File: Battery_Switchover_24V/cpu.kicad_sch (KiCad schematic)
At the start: 35 parts, among them J1 USB_C_Receptacle_USB2.0_14P, M1 Fan, Q1 NPN, SW1 SW_Push, U1 OPA2197xD, U2 OPA2197xD, U3 LPC11U14FBD48-201, Y1 12.000MHz

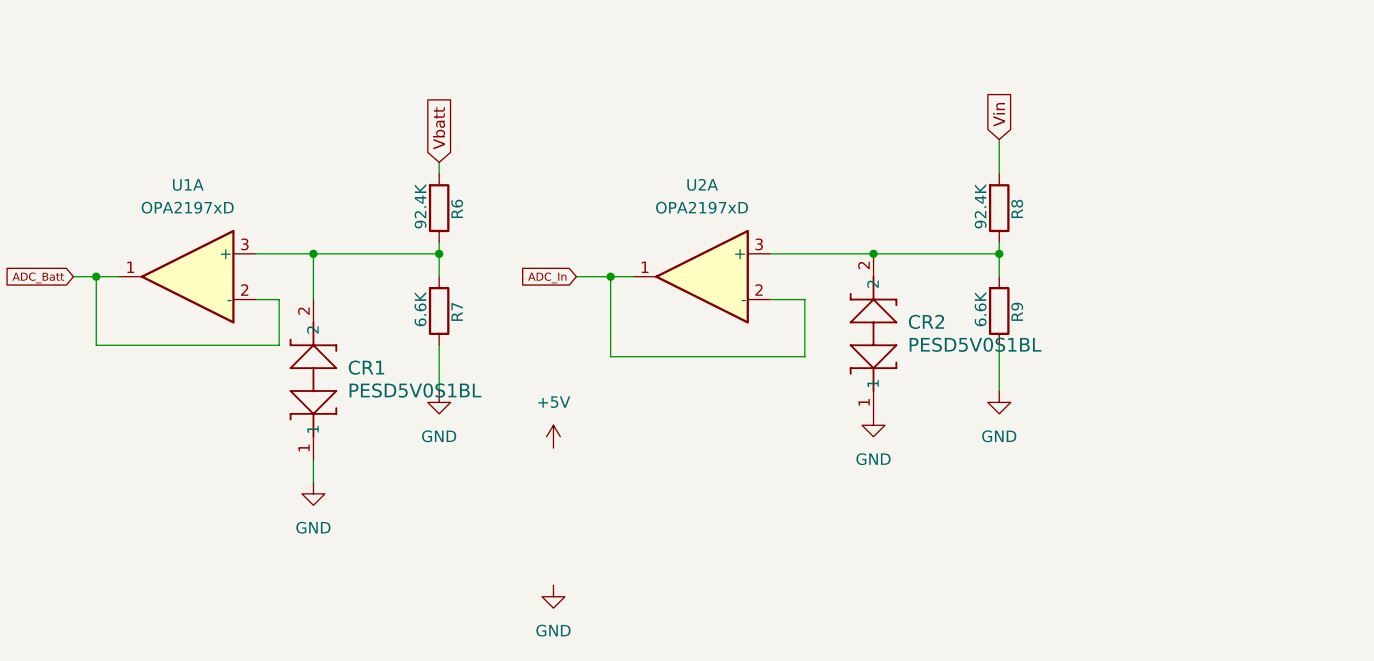
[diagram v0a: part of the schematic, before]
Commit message: Added common mode chokes for input and output of the load fixed the corrupted board
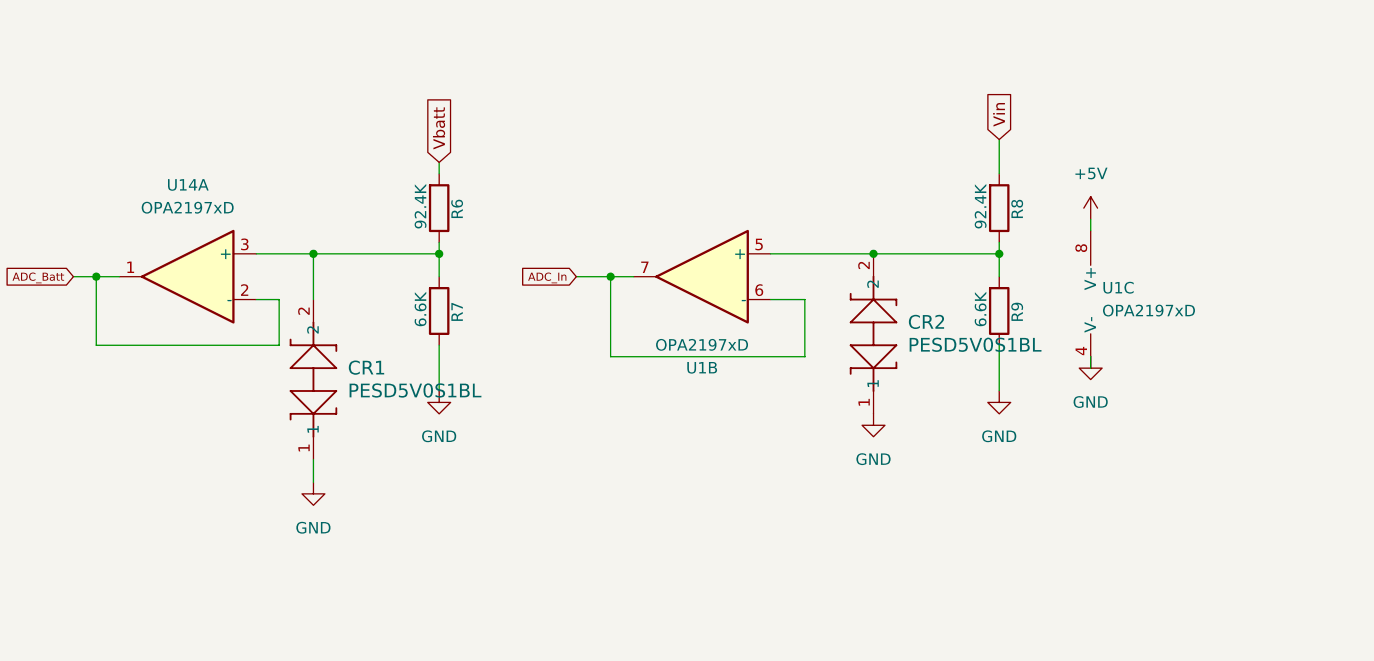
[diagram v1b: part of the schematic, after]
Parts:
- removed U1, U2: OPA2197xD, Package_SO:SOIC-8_3.9x4.9mm_P1.27mm, symbol Amplifier_Operational:OPA2197xD
- added U1, U14: OPA2197xD, Package_SO:SOIC-8_3.9x4.9mm_P1.27mm, symbol Amplifier_Operational:OPA2197xD
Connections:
- net +5V: now also U1.8 (V+)
- net ADC_Batt: now also U14.1, U14.2 (-)
- net ADC_In: now also U1.6 (-), U1.7
- net GND: now also U1.4 (V-)
- net at CR2.2, R8.1, R9.2: now also U1.5 (+)
- net at CR1.2, R6.1, R7.2: now also U14.3 (+)

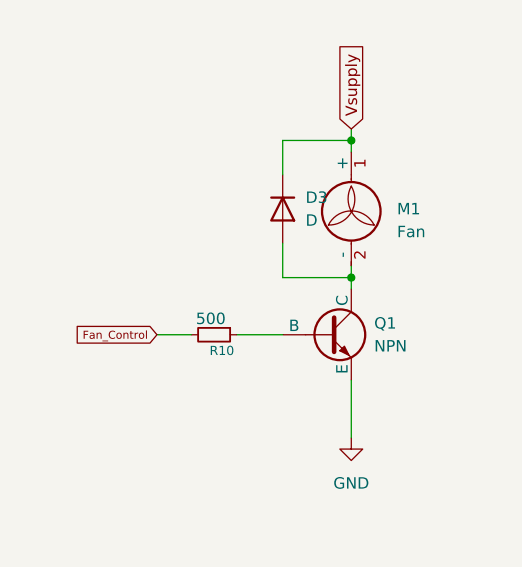
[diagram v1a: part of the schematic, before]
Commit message: Added Footprints to the remaining parts calculated the current IC's resistance and capcitances
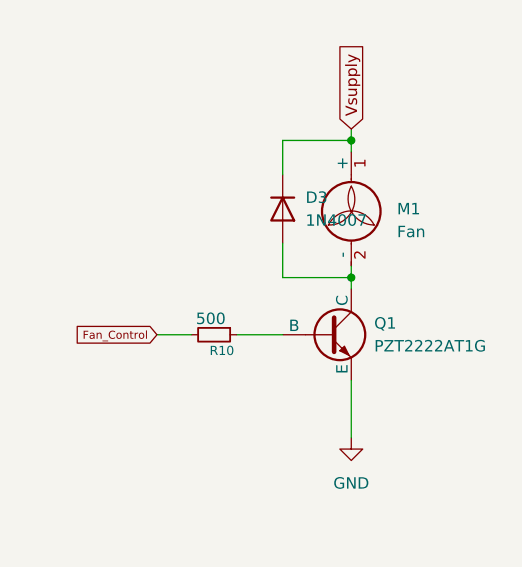
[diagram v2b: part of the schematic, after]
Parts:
- C6, C7: footprint (none) -> Capacitor_THT:C_Radial_D8.0mm_H7.0mm_P3.50mm
- D2, D4, D5: footprint (none) -> LED_SMD:LED_0805_2012Metric_Pad1.15x1.40mm_HandSolder
- D3: value D -> 1N4007; footprint (none) -> Diode_THT:D_5W_P10.16mm_Horizontal
- M1: footprint (none) -> Connector_PinHeader_2.54mm:PinHeader_1x02_P2.54mm_Vertical
- Q1: value NPN -> PZT2222AT1G; footprint (none) -> Package_TO_SOT_SMD:SOT-223-3_TabPin2
- SW1: footprint (none) -> Button_Switch_SMD:SW_SPST_TL3305A
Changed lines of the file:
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@@
 			)
 		)
-		(property "Value" "NPN"
+		(property "Value" "PZT2222AT1G"
 			(at 278.13 144.7799 0)
 			(effects
@@
 			)
 		)
-		(property "Footprint" ""
+		(property "Footprint" "Package_TO_SOT_SMD:SOT-223-3_TabPin2"
 			(at 336.55 143.51 0)
 			(effects
@@
 			)
 		)
-		(property "Value" "D"
+		(property "Value" "1N4007"
 			(at 270.51 130.8099 90)
 			(effects
@@
 			)
 		)
-		(property "Footprint" ""
+		(property "Footprint" "Diode_THT:D_5W_P10.16mm_Horizontal"
 			(at 267.97 129.54 0)
 			(effects
@@
 			)
 		)
-		(property "Footprint" ""
+		(property "Footprint" "LED_SMD:LED_0805_2012Metric_Pad1.15x1.40mm_HandSolder"
 			(at 264.16 69.85 0)
 			(effects
@@
 			)
 		)
-		(property "Datasheet" "~"
+		(property "Datasheet" "HL-PSC-2012S9AC"
 			(at 264.16 69.85 0)
 			(effects
@@
 			)
 		)
-		(property "Footprint" ""
+		(property "Footprint" "Connector_PinHeader_2.54mm:PinHeader_1x02_P2.54mm_Vertical"
 			(at 275.59 130.556 0)
 			(effects
@@
 			)
 		)
-		(property "Footprint" ""
+		(property "Footprint" "Capacitor_THT:C_Radial_D8.0mm_H7.0mm_P3.50mm"
 			(at 201.93 24.13 0)
 			(effects
@@
 			)
 		)
-		(property "Footprint" ""
+		(property "Footprint" "LED_SMD:LED_0805_2012Metric_Pad1.15x1.40mm_HandSolder"
 			(at 271.78 69.85 0)
 			(effects
@@
 			)
 		)
-		(property "Footprint" ""
+		(property "Footprint" "Capacitor_THT:C_Radial_D8.0mm_H7.0mm_P3.50mm"
 			(at 194.31 24.13 0)
 			(effects
@@
 			)
 		)
-		(property "Footprint" ""
+		(property "Footprint" "Button_Switch_SMD:SW_SPST_TL3305A"
 			(at 41.91 16.51 0)
 			(effects
@@
 			)
 		)
-		(property "Footprint" ""
+		(property "Footprint" "LED_SMD:LED_0805_2012Metric_Pad1.15x1.40mm_HandSolder"
 			(at 279.4 69.85 0)
 			(effects

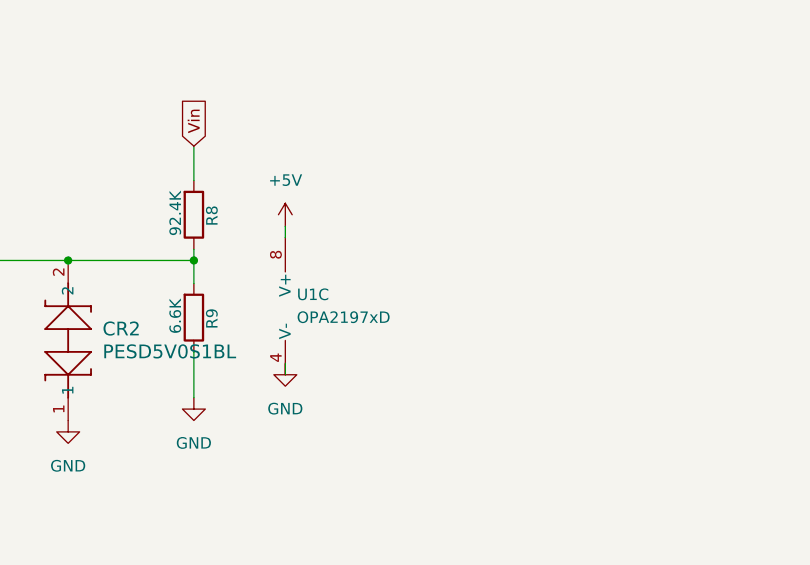
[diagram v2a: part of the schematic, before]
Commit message: Added board edge to PCB and some general placement as well as some schematic changes
Added connectors for Vin and for low side current monitoring(3 connectors) (connector types must be changed. Changes to the power controll circuit added bypass capacitor to the opamp. Added output connector
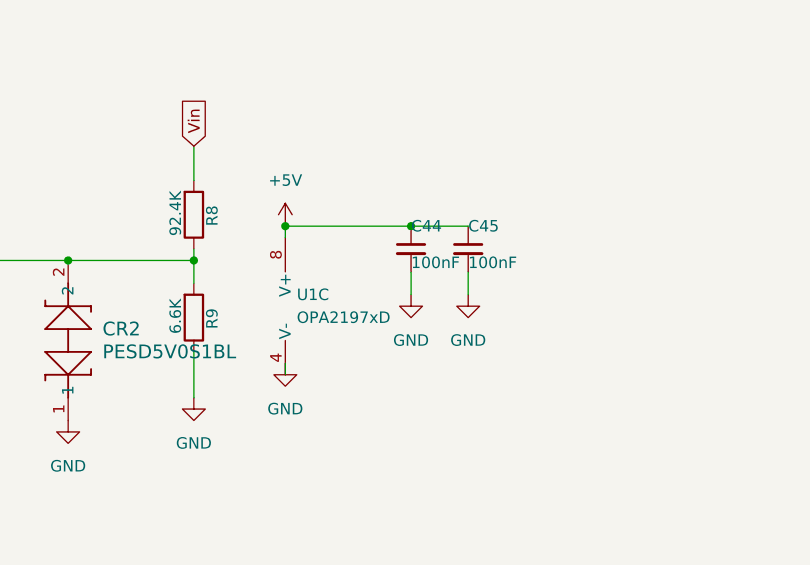
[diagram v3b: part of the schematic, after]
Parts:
- added C44, C45: 100nF, Capacitor_SMD:C_0603_1608Metric, symbol Device:C_Small
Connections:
- net +5V: now also C44.1, C45.1
- net GND: now also C44.2, C45.2

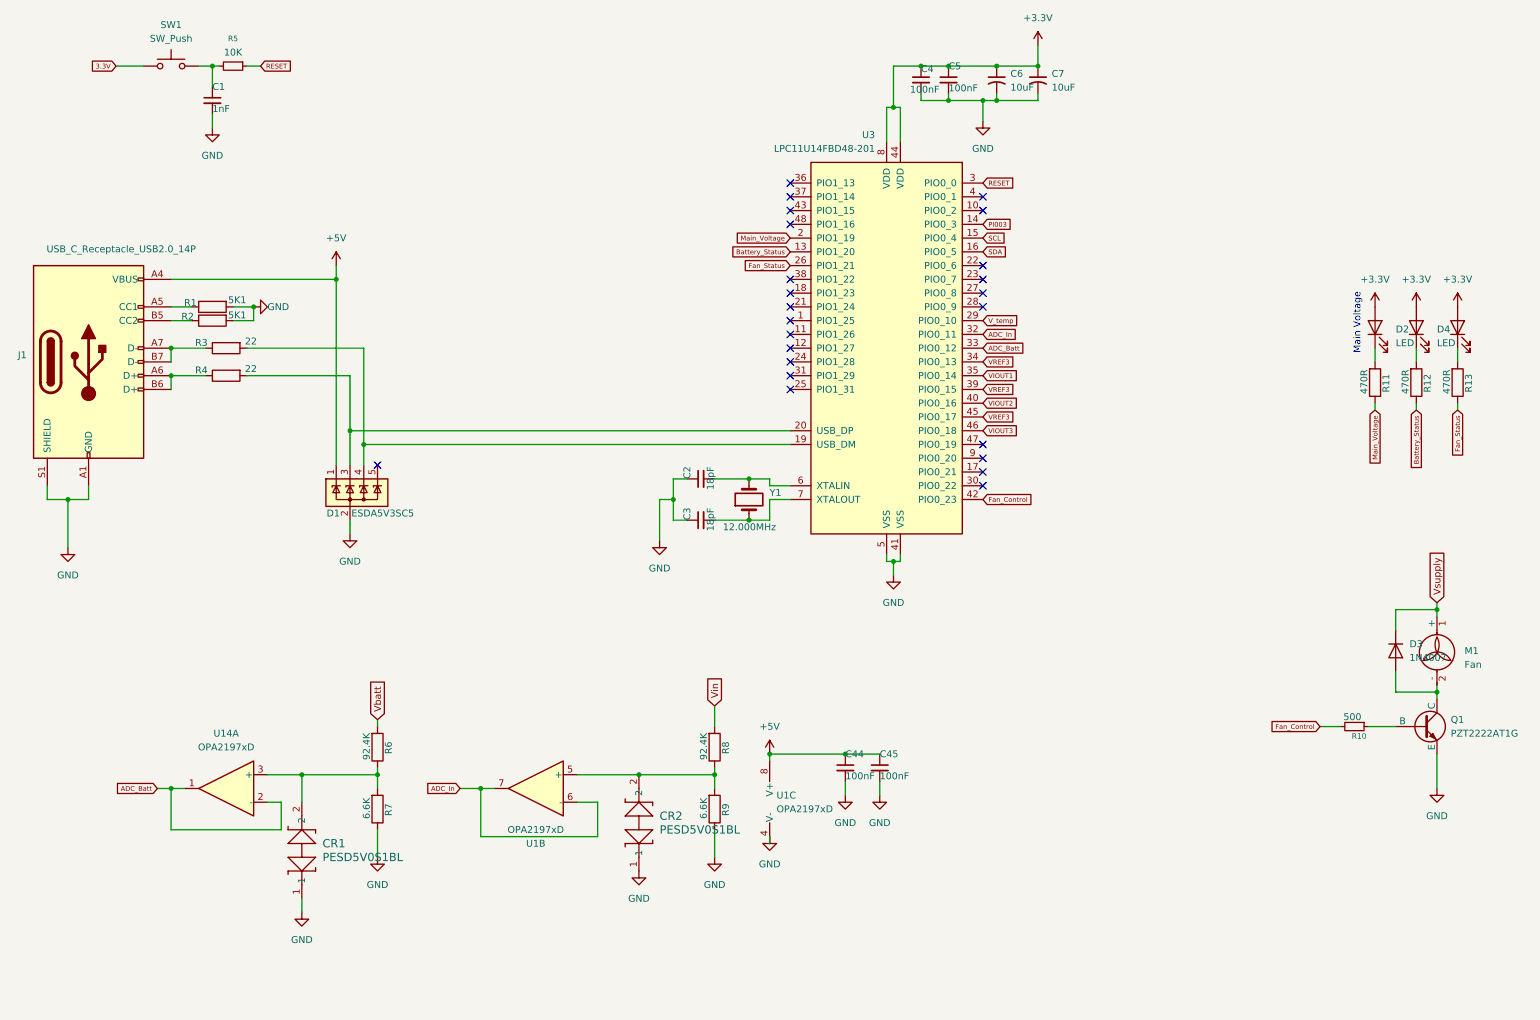
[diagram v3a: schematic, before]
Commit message: Fixed opamp footprint issue done some preliminary placement
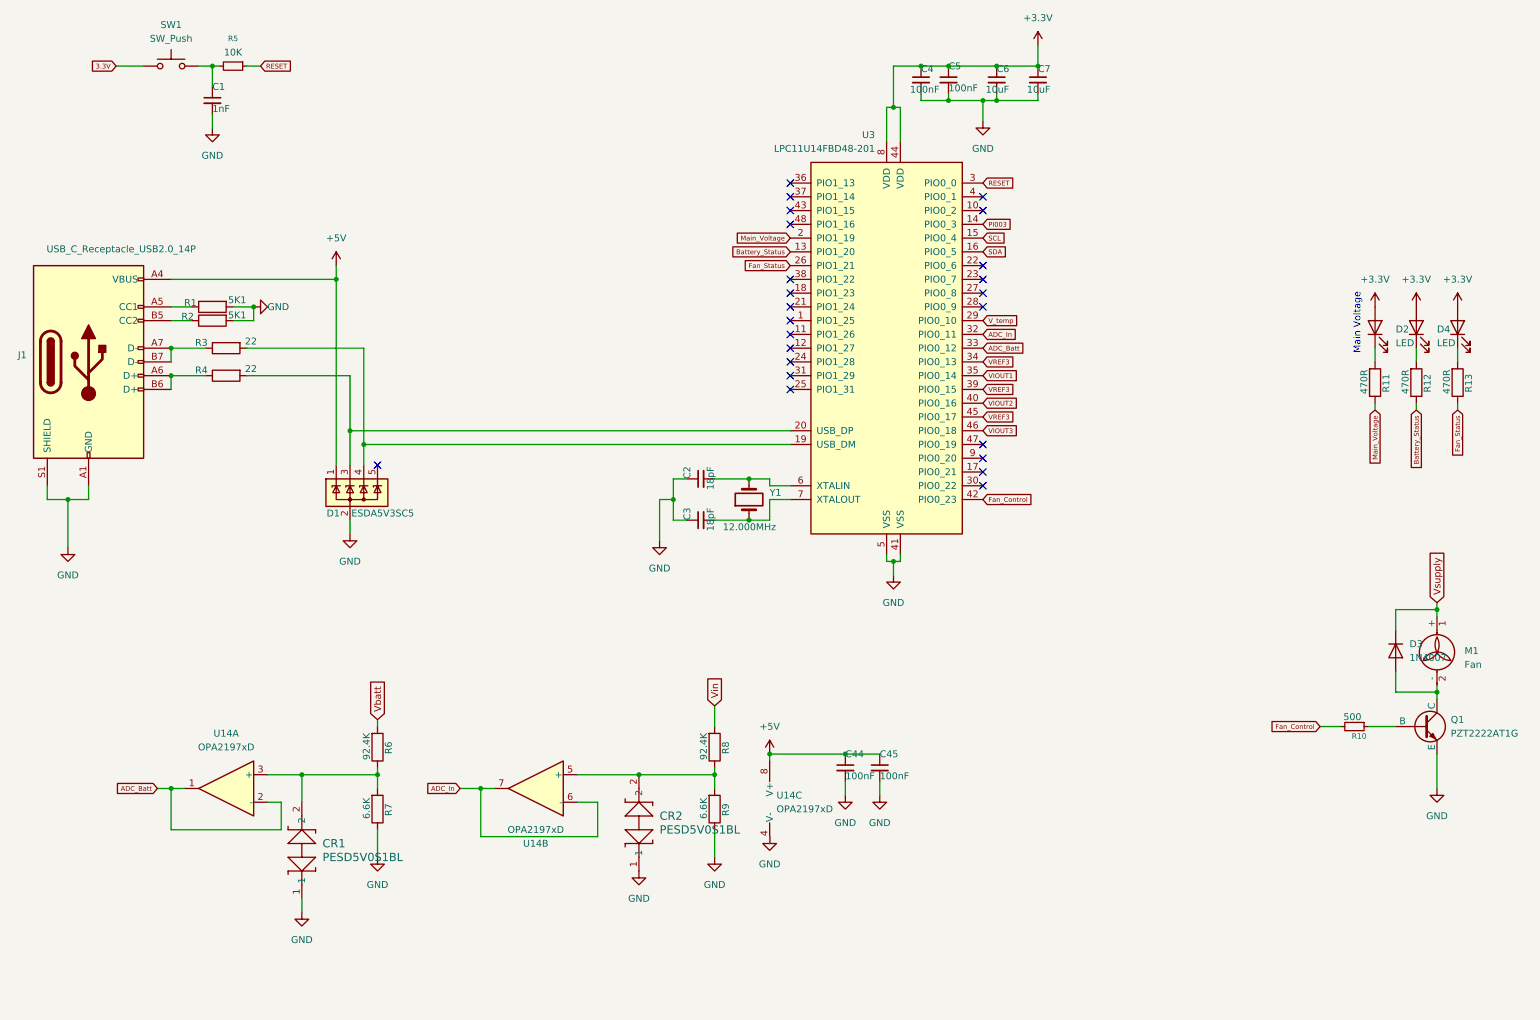
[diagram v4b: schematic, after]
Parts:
- removed C6, C7: 10uF, Capacitor_THT:C_Radial_D8.0mm_H7.0mm_P3.50mm, symbol Device:C_Small_US
- removed U1: OPA2197xD, Package_SO:SOIC-8_3.9x4.9mm_P1.27mm, symbol Amplifier_Operational:OPA2197xD
- added C6, C7: 10uF, Capacitor_SMD:C_0603_1608Metric, symbol Device:C_Small
- added unit 2 of U14
- added unit 3 of U14
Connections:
- net +3.3V: now also C6.1, C7.1
- net +5V: now also U14.8 (V+)
- net ADC_In: now also U14.6 (-), U14.7
- net GND: now also C6.2, C7.2, U14.4 (V-)
- net at CR2.2, R8.1, R9.2: now also U14.5 (+)

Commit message: Added 6 Pin ATX Connector
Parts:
- J1: footprint Connector_USB:USB_C_Receptacle_G-Switch_GT-USB-7010ASV -> Connector_USB:USB_C_Receptacle_G-Switch_GT-USB-7051x
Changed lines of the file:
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@@
 			)
 		)
-		(property "Footprint" "Connector_USB:USB_C_Receptacle_G-Switch_GT-USB-7010ASV"
+		(property "Footprint" "Connector_USB:USB_C_Receptacle_G-Switch_GT-USB-7051x"
 			(at 30.48 76.2 0)
 			(effects

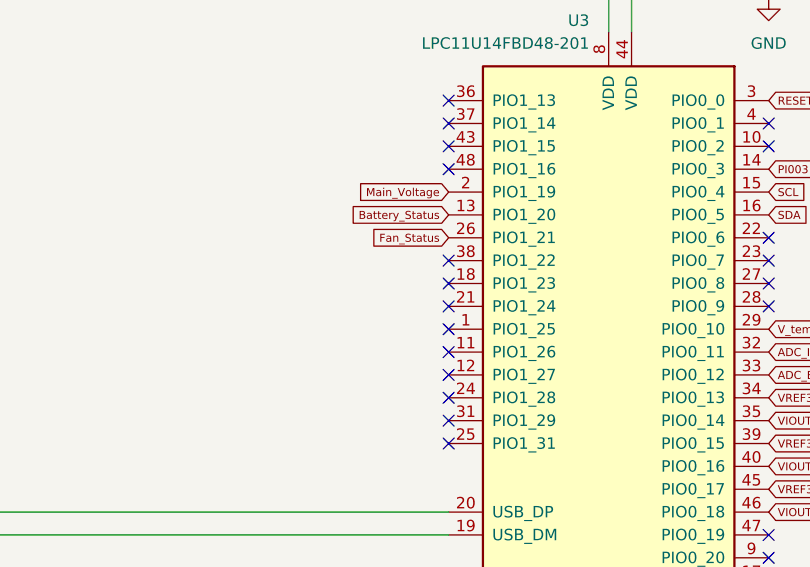
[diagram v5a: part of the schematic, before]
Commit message: Added DS18B20 Temperature sensor
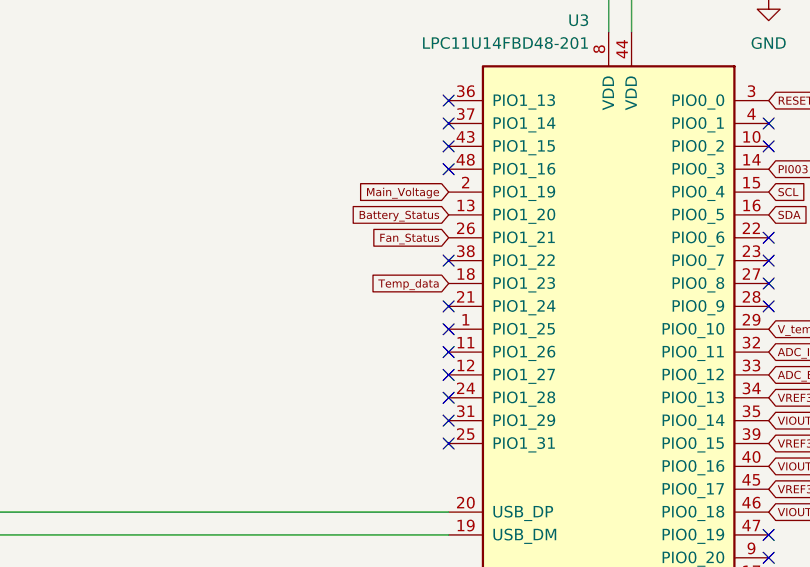
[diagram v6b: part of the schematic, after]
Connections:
- net Temp_data: now reaches U3.18 (PIO1_23)
- no-connect marks 24 -> 23
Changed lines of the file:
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@@
-	)
-	(no_connect
-		(at 156.21 63.5)
 	)
 	(no_connect
@@
 				(hide yes)
 			)
+		)
+	)
+	(global_label "Temp_data"
+		(shape input)
+		(at 156.21 63.5 180)
+		(fields_autoplaced yes)
+		(effects
+			(font
+				(size 0.889 0.889)
+			)
+			(justify right)
+		)
+		(property "Intersheetrefs" "${INTERSHEET_REFS}"
+			(at 147.0934 63.5 0)
+			(effects
+				(font
+					(size 1.27 1.27)
+				)
+				(justify right)
+				(hide yes)
+			)
